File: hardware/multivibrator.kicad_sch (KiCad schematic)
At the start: 9 parts, among them J1 KLS2-EDR-5.08-02P-4

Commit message: Создана схема
Изменена структура проекта
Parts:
- renumbered VT1 to Q1, VT2 to Q2
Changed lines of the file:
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@@
 		(dnp no)
 		(fields_autoplaced yes)
-		(property "Reference" "VT2"
+		(property "Reference" "Q2"
 			(at 125.73 72.3899 0)
 			(effects
@@
 			(project ""
 				(path "/1a97188f-c325-4cd3-a978-b976f5ea7e32"
-					(reference "VT2")
+					(reference "Q2")
 					(unit 1)
 				)
@@
 		(on_board yes)
 		(dnp no)
-		(property "Reference" "VT1"
+		(property "Reference" "Q1"
 			(at 82.55 72.3899 0)
 			(effects
@@
 			(project "multivibrator"
 				(path "/1a97188f-c325-4cd3-a978-b976f5ea7e32"
-					(reference "VT1")
+					(reference "Q1")
 					(unit 1)
 				)

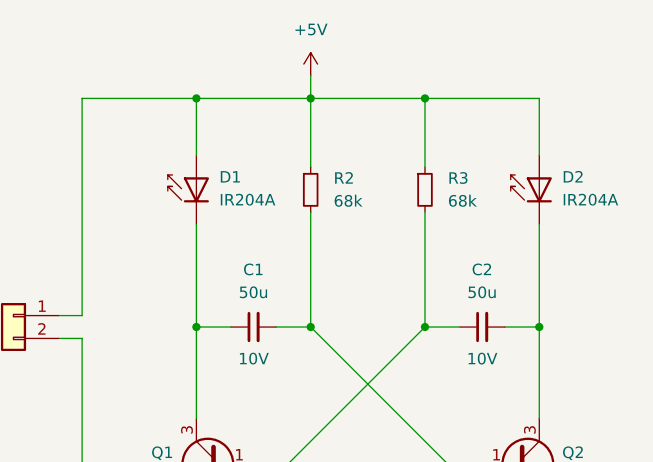
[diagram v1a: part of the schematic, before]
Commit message: Создана печатная плата
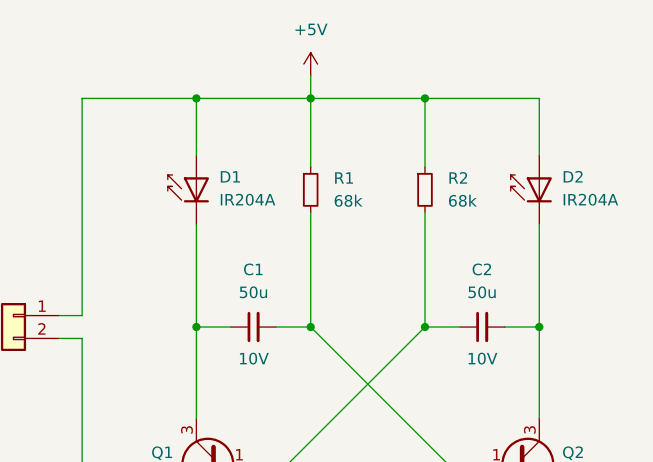
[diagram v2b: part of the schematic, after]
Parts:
- renumbered R2 to R1, R3 to R2
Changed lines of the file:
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@@
 		(dnp no)
 		(fields_autoplaced yes)
-		(property "Reference" "R3"
+		(property "Reference" "R2"
 			(at 113.03 41.9099 0)
 			(effects
@@
 			(project "multivibrator"
 				(path "/1a97188f-c325-4cd3-a978-b976f5ea7e32"
-					(reference "R3")
+					(reference "R2")
 					(unit 1)
 				)
@@
 		(dnp no)
 		(fields_autoplaced yes)
-		(property "Reference" "R2"
+		(property "Reference" "R1"
 			(at 100.33 41.9099 0)
 			(effects
@@
 			(project "multivibrator"
 				(path "/1a97188f-c325-4cd3-a978-b976f5ea7e32"
-					(reference "R2")
+					(reference "R1")
 					(unit 1)
 				)

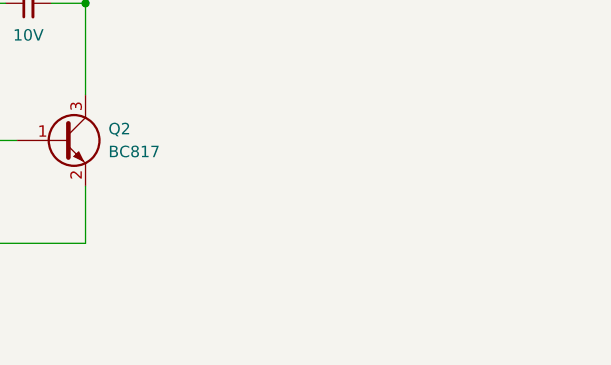
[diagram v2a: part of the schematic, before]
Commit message: Добавлены монтажные отверстия
+ изменена структура репозитория
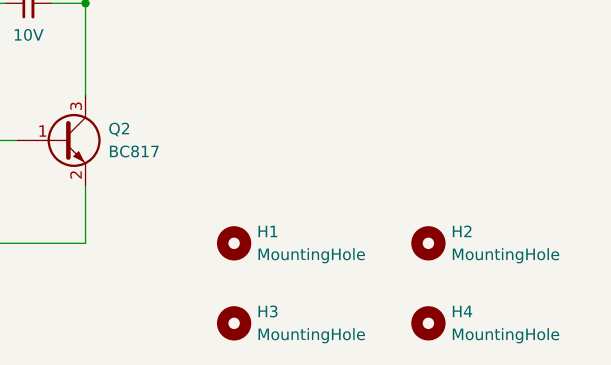
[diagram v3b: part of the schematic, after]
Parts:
- added H1, H2, H3, H4: MountingHole, MountingHole:MountingHole_2.2mm_M2, symbol Mechanical:MountingHole

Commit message: учтены замечания
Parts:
- removed H1, H2, H3, H4: MountingHole, MountingHole:MountingHole_2.2mm_M2, symbol Mechanical:MountingHole
- added H1, H2, H3, H4: MountingHole_Pad, MountingHole:MountingHole_3.2mm_M3_DIN965_Pad, symbol Mechanical:MountingHole_Pad
- C1, C2: value 50u -> 47u; chipdip (none) -> 9000326168
- D1, D2: chipdip (none) -> 8003472582
- J1: chipdip (none) -> 9000603329
- Q1, Q2: chipdip (none) -> 28806907
- R1, R2: chipdip (none) -> 9000189877

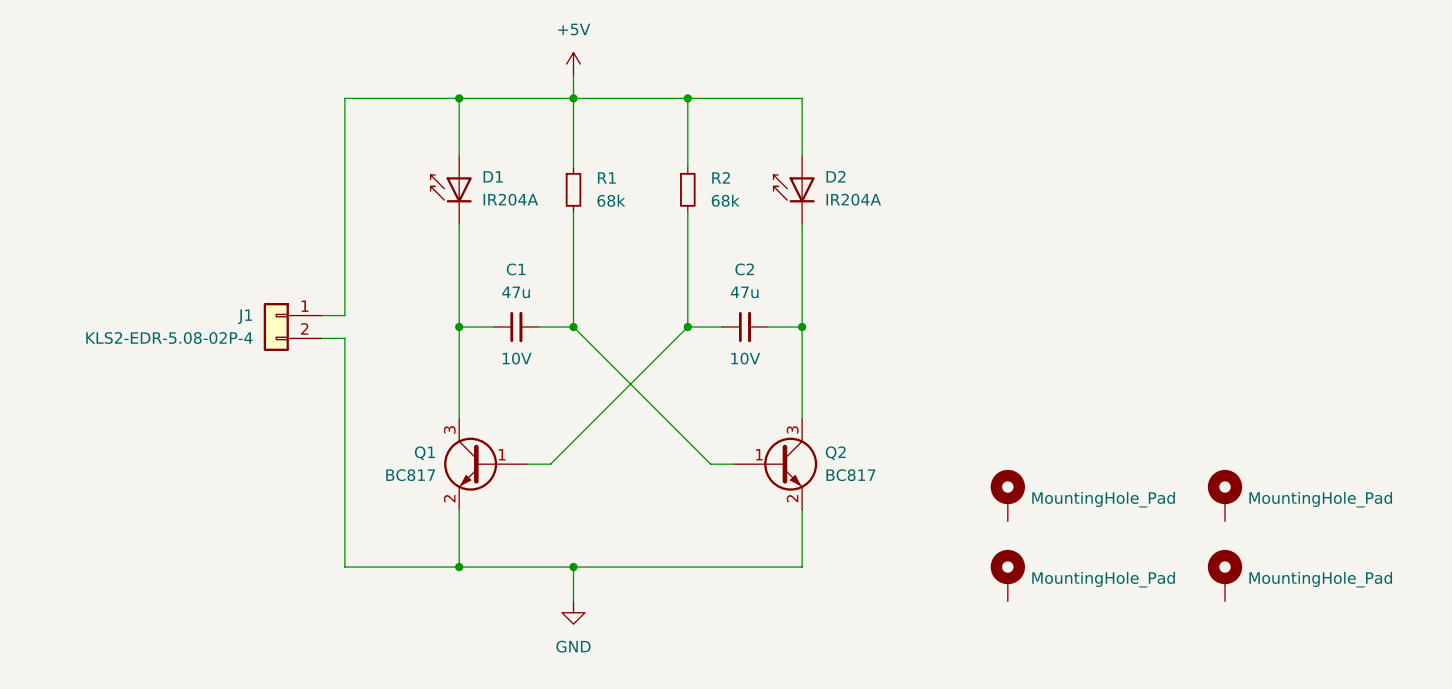
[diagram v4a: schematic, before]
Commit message: приняты новые рекомендации
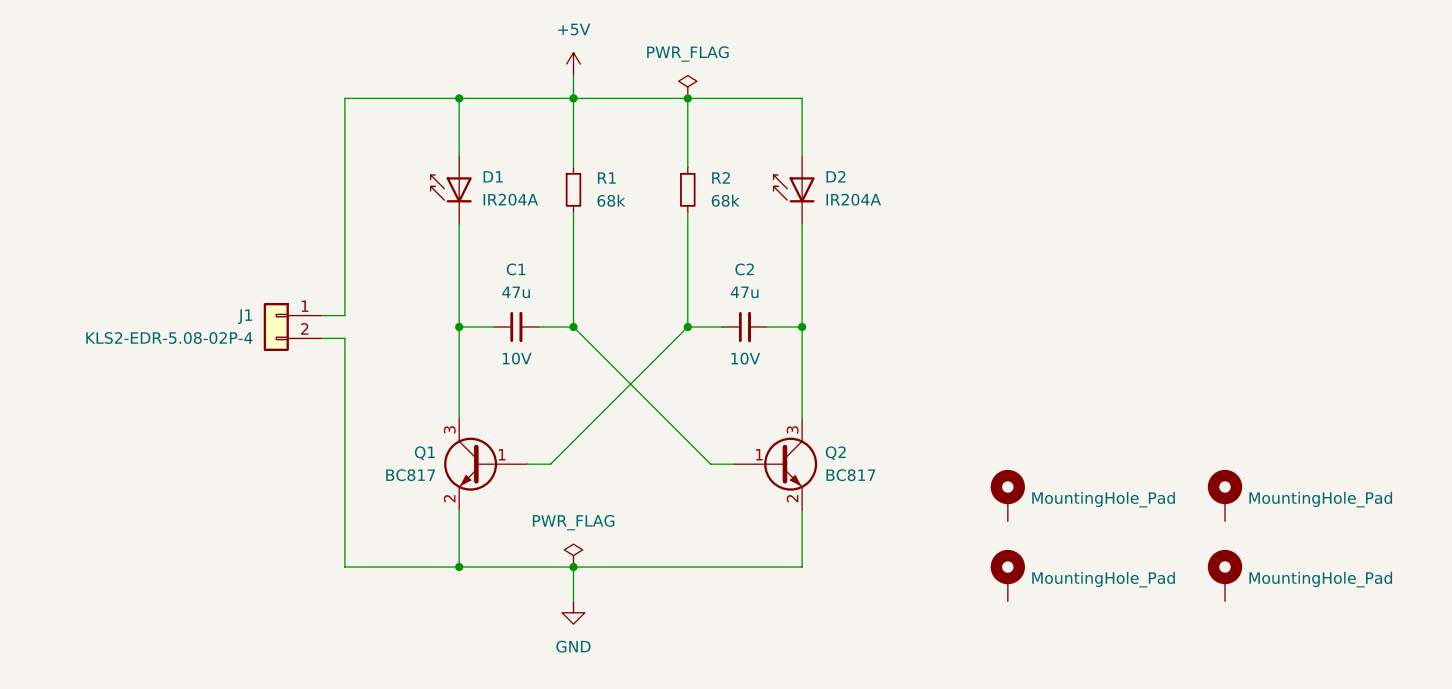
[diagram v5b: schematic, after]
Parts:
- C1, C2: lcsc (none) -> C6119904
- D1, D2: chipdip 8003472582 -> 8023113118; lcsc (none) -> C264278
- Q1, Q2: lcsc (none) -> C5249694
- R1, R2: lcsc (none) -> C17801
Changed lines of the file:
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@@
 			)
 		)
-		(property "lcsc" ""
+		(property "lcsc" "C17801"
 			(at 110.49 43.18 0)
 			(effects
@@
 			)
 		)
-		(property "chipdip" "8003472582"
+		(property "chipdip" "8023113118"
+			(at 123.19 41.91 0)
+			(effects
+				(font
+					(size 1.27 1.27)
+				)
+				(hide yes)
+			)
+		)
+		(property "lcsc" "C264278"
 			(at 123.19 41.91 0)
 			(effects
@@
 			)
 		)
-		(property "lcsc" ""
+		(property "lcsc" " C5249694"
 			(at 120.65 73.66 0)
 			(effects
@@
 	)
 	(symbol
+		(lib_id "power:PWR_FLAG")
+		(at 110.49 33.02 0)
+		(unit 1)
+		(exclude_from_sim no)
+		(in_bom yes)
+		(on_board yes)
+		(dnp no)
+		(property "Reference" "#FLG01"
+			(at 110.49 31.115 0)
+			(effects
+				(font
+					(size 1.27 1.27)
+				)
+				(hide yes)
+			)
+		)
+		(property "Value" "PWR_FLAG"
+			(at 110.49 27.94 0)
+			(effects
+				(font
+					(size 1.27 1.27)
+				)
+			)
+		)
+		(property "Footprint" ""
+			(at 110.49 33.02 0)
+			(effects
+				(font
+					(size 1.27 1.27)
+				)
+				(hide yes)
+			)
+		)
+		(property "Datasheet" "~"
+			(at 110.49 33.02 0)
+			(effects
+				(font
+					(size 1.27 1.27)
+				)
+				(hide yes)
+			)
+		)
+		(property "Description" "Special symbol for telling ERC where power comes from"
+			(at 110.49 33.02 0)
+			(effects
+				(font
+					(size 1.27 1.27)
+				)
+				(hide yes)
+			)
+		)
+		(pin "1"
+		)
+		(instances
+			(project ""
+				(path "/1a97188f-c325-4cd3-a978-b976f5ea7e32"
+					(reference "#FLG01")
+					(unit 1)
+				)
+			)
+		)
+	)
+	(symbol
 		(lib_id "LED:IR204A")
 		(at 85.09 41.91 90)
@@
 			)
 		)
-		(property "chipdip" "8003472582"
+		(property "chipdip" "8023113118"
+			(at 85.09 41.91 0)
+			(effects
+				(font
+					(size 1.27 1.27)
+				)
+				(hide yes)
+			)
+		)
+		(property "lcsc" "C264278"
 			(at 85.09 41.91 0)
 			(effects
@@
 			)
 		)
-		(property "lcsc" ""
+		(property "lcsc" "C6119904"
 			(at 116.84 58.42 0)
 			(effects
@@
 				(path "/1a97188f-c325-4cd3-a978-b976f5ea7e32"
 					(reference "C2")
+					(unit 1)
+				)
+			)
+		)
+	)
+	(symbol
+		(lib_id "power:PWR_FLAG")
+		(at 97.79 85.09 0)
+		(unit 1)
+		(exclude_from_sim no)
+		(in_bom yes)
+		(on_board yes)
+		(dnp no)
+		(fields_autoplaced yes)
+		(property "Reference" "#FLG02"
+			(at 97.79 83.185 0)
+			(effects
+				(font
+					(size 1.27 1.27)
+				)
+				(hide yes)
+			)
+		)
+		(property "Value" "PWR_FLAG"
+			(at 97.79 80.01 0)
+			(effects
+				(font
+					(size 1.27 1.27)
+				)
+			)
+		)
+		(property "Footprint" ""
+			(at 97.79 85.09 0)
+			(effects
+				(font
+					(size 1.27 1.27)
+				)
+				(hide yes)
+			)
+		)
+		(property "Datasheet" "~"
+			(at 97.79 85.09 0)
+			(effects
+				(font
+					(size 1.27 1.27)
+				)
+				(hide yes)
+			)
+		)
+		(property "Description" "Special symbol for telling ERC where power comes from"
+			(at 97.79 85.09 0)
+			(effects
+				(font
+					(size 1.27 1.27)
+				)
+				(hide yes)
+			)
+		)
+		(pin "1"
+		)
+		(instances
+			(project ""
+				(path "/1a97188f-c325-4cd3-a978-b976f5ea7e32"
+					(reference "#FLG02")
 					(unit 1)
 				)
@@
 			)
 		)
-		(property "lcsc" ""
+		(property "lcsc" " C5249694"
 			(at 87.63 73.66 0)
 			(effects
@@
 			)
 		)
-		(property "lcsc" ""
+		(property "lcsc" "C6119904"
 			(at 91.44 58.42 0)
 			(effects
@@
 			)
 		)
-		(property "lcsc" ""
+		(property "lcsc" "C17801"
 			(at 97.79 43.18 0)
 			(effects
@@
 	)
 	(symbol
+		(lib_name "MountingHole_Pad_1")
 		(lib_id "Mechanical:MountingHole_Pad")
 		(at 146.05 77.47 0)
